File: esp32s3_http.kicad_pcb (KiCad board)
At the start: 2 copper layers, 55 x 90 mm, 43 parts, among them J1 USB_B, J2 Jack-DC, J3 UART0, SW1 SW_Push, SW2 SW_Push, U1 ESP32-S3-WROOM-1, U2 LM2940T-3.3, U3 NJM7805FA, Y1 32.768KHz

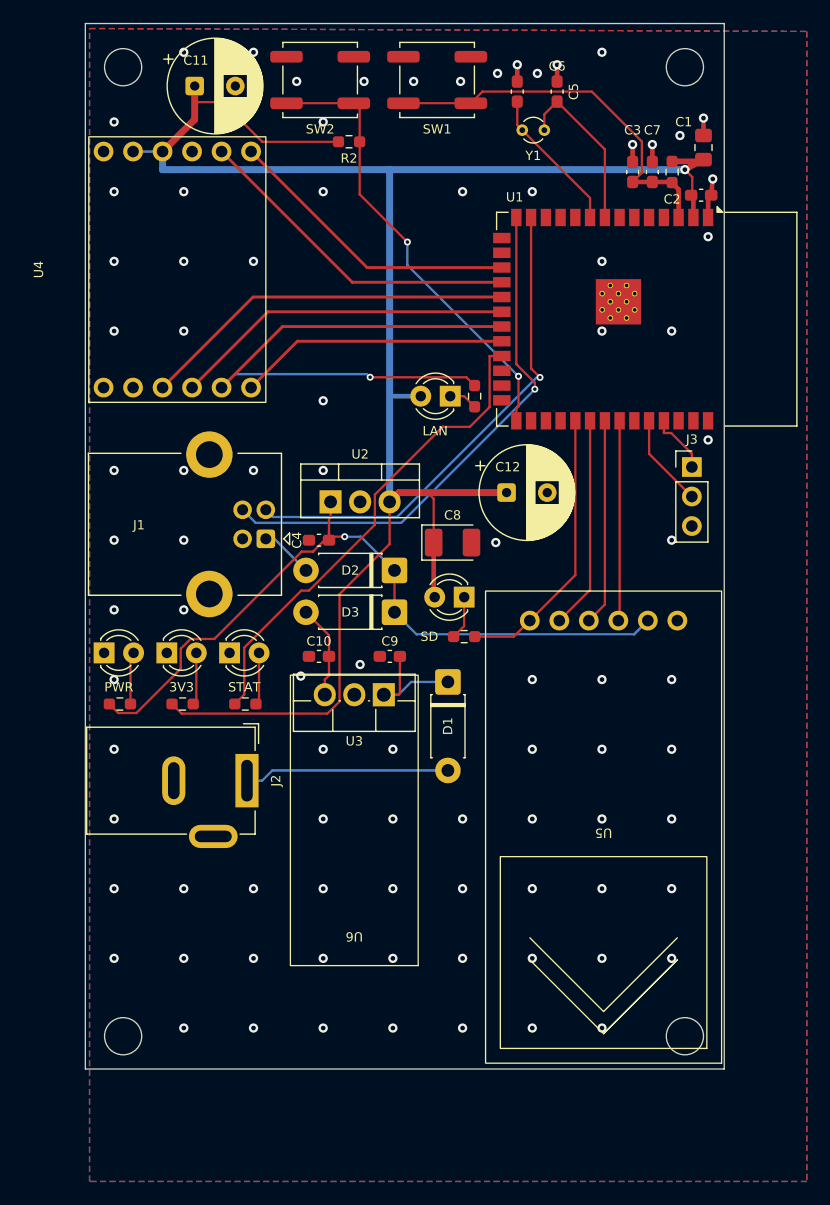
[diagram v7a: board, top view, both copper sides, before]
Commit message: PCB: GPIO ヘッダ J3(2x4)/J4(2x6) 追加、ボタンを左下へ移動
- J4 を上端 (旧ボタン位置) に、J3 を U1 右下に配置、ピン名をシルク表示
- SW1/SW2/R2 を左下へ、EN は B.Cu で基板外周を固定配線

Co-Authored-By: Claude Opus 5.5 <noreply@anthropic.com>
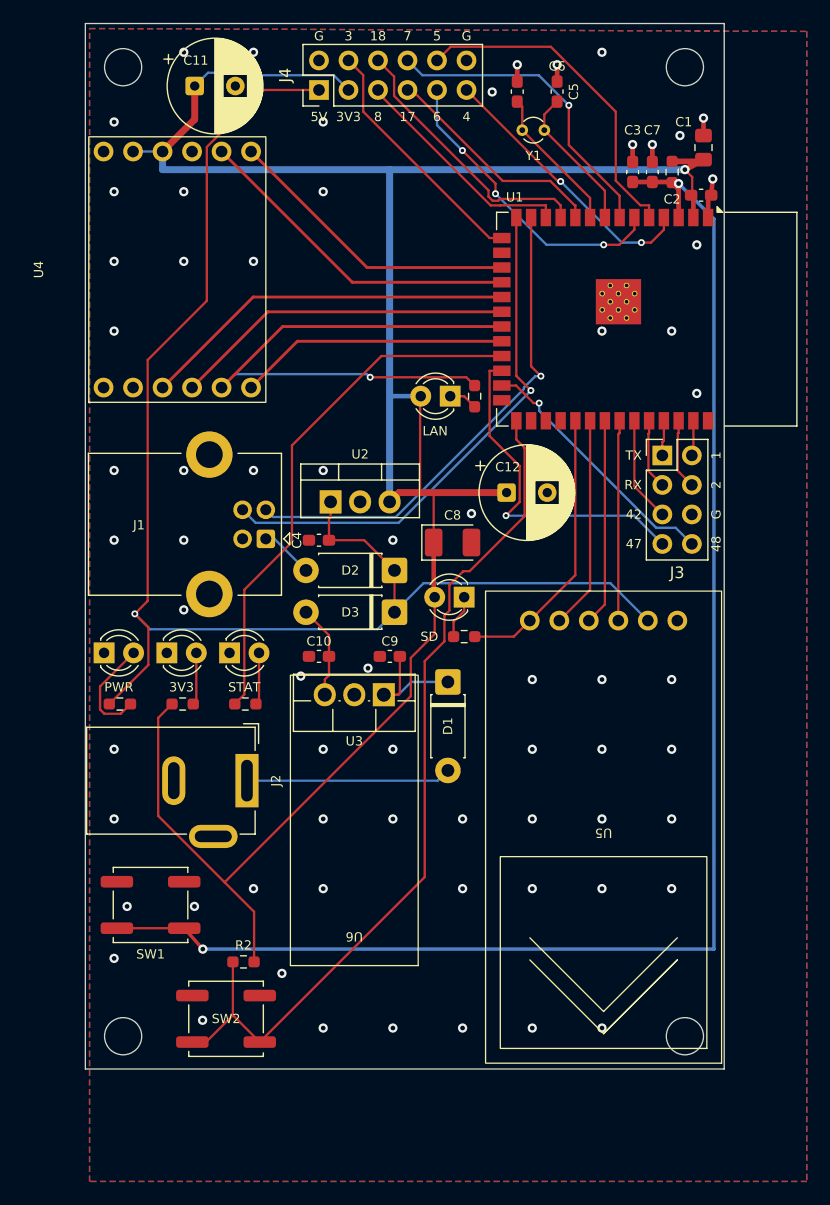
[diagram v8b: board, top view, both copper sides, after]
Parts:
- added J4: EXP2, Connector_PinHeader_2.54mm:PinHeader_2x06_P2.54mm_Vertical, F.Cu at (57.5, 70.5)
- J3: value UART0 -> EXP1_UART; footprint Connector_PinHeader_2.54mm:PinHeader_1x03_P2.54mm_Vertical -> Connector_PinHeader_2.54mm:PinHeader_2x04_P2.54mm_Vertical
- moved SW2 81.2 mm to (49.5, 150.5)
- moved SW1 75.2 mm to (43.0, 140.7)
- moved R2 71.2 mm to (51.0, 145.6), turned to 0 degrees
- moved J3 2.73 mm to (87.1, 102.0)
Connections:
- J3 pad 2: U0RXD -> GPIO1
- J3 pad 3: GND -> U0RXD
- U1 pad 10: unconnected-(U1-IO17-Pad10) -> GPIO17
- U1 pad 11: unconnected-(U1-IO18-Pad11) -> GPIO18
- U1 pad 12: unconnected-(U1-IO8-Pad12) -> GPIO8
- U1 pad 15: unconnected-(U1-IO3-Pad15) -> GPIO3
- U1 pad 24: unconnected-(U1-IO47-Pad24) -> GPIO47
- U1 pad 25: unconnected-(U1-IO48-Pad25) -> GPIO48
- U1 pad 35: unconnected-(U1-IO42-Pad35) -> GPIO42
- U1 pad 38: unconnected-(U1-IO2-Pad38) -> GPIO2
- U1 pad 39: unconnected-(U1-IO1-Pad39) -> GPIO1
- U1 pad 4: unconnected-(U1-IO4-Pad4) -> GPIO4
- U1 pad 5: unconnected-(U1-IO5-Pad5) -> GPIO5
- U1 pad 6: unconnected-(U1-IO6-Pad6) -> GPIO6
- U1 pad 7: unconnected-(U1-IO7-Pad7) -> GPIO7
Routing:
- net EN: track 33.2 -> 126.4 mm, vias 0 -> 2
- net 5V: track 64.0 -> 125.4 mm
- net BOOT: track 39.1 -> 75.8 mm, vias 2 -> 0
- net VDD33: track 164.0 -> 196.7 mm
- net GPIO47: track 0.00 -> 29.5 mm, vias 0 -> 1
- net GPIO5: track 0.00 -> 28.9 mm
- net GPIO7: track 0.00 -> 27.0 mm, vias 0 -> 1
- net GPIO6: track 0.00 -> 26.4 mm, vias 0 -> 3
- net GPIO4: track 0.00 -> 23.9 mm, vias 0 -> 2
- net GPIO18: track 0.00 -> 23.4 mm
- net GPIO48: track 0.00 -> 22.4 mm, vias 0 -> 1
- net GPIO3: track 0.00 -> 21.4 mm
- net GPIO8: track 0.00 -> 19.8 mm
- net GPIO17: track 0.00 -> 19.6 mm
- net GPIO42: track 0.00 -> 9.06 mm
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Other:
- board text added: "1"
- board text added: "17"
- board text added: "18"
- board text added: "2"
- board text added: "3"
- board text added: "4"
- board text added: "42"
- board text added: "47"
- board text added: "48"
- board text added: "5"
- board text added: "5V"
- board text added: "6"
- board text added: "7"
- board text added: "8"
- board text added: "G"
- board text added: "RX"
- board text added: "TX"
